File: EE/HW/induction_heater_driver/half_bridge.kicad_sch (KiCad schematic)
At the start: 7 parts, among them Q1 BSC0702LSATMA1, Q2 IRFB7534PBF, U1 UCC5304DWVR

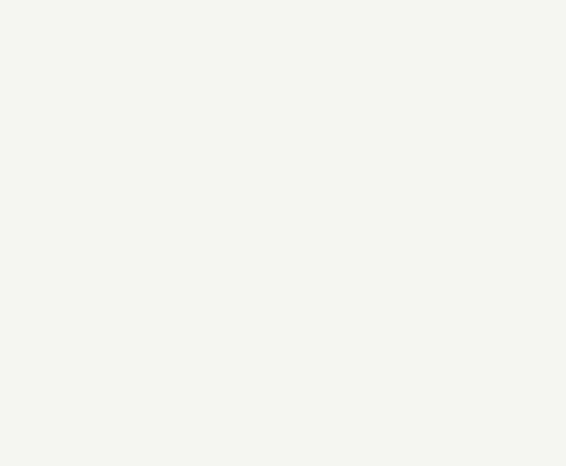
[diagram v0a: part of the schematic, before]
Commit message: imported MAG package from github
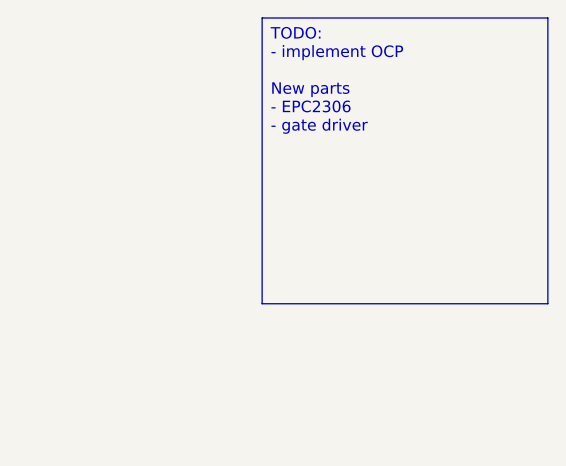
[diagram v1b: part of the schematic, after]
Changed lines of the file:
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@@
 	(generator_version "9.0")
 	(paper "A4")
+	(text_box "TODO:\n- implement OCP\n\nNew parts \n- EPC2306\n- gate driver"
+		(exclude_from_sim no)
+		(at 231.14 30.48 0)
+		(size 31.75 31.75)
+		(margins 0.9525 0.9525 0.9525 0.9525)
+		(stroke
+			(width 0)
+			(type solid)
+		)
+		(fill
+			(type none)
+		)
+		(effects
+			(font
+				(size 1.27 1.27)
+			)
+			(justify left top)
+		)
+	)
 	(symbol
 		(lib_id "peml_passives:CRCW06031R00FKEAHP")
@@
 		)
 		(instances
-			(project ""
+			(project "induction_heater_driver"
 				(path "/4a4d350d-8886-4083-afc6-4b49fb4e1662/876ef4ab-98e7-4587-95f9-89debc1f72ad"
 					(reference "Q2")
@@
 		)
 		(instances
-			(project ""
+			(project "induction_heater_driver"
 				(path "/4a4d350d-8886-4083-afc6-4b49fb4e1662/876ef4ab-98e7-4587-95f9-89debc1f72ad"
 					(reference "R1")
@@
 		)
 		(instances
-			(project ""
+			(project "induction_heater_driver"
 				(path "/4a4d350d-8886-4083-afc6-4b49fb4e1662/876ef4ab-98e7-4587-95f9-89debc1f72ad"
 					(reference "C4")
@@
 		)
 		(instances
-			(project ""
+			(project "induction_heater_driver"
 				(path "/4a4d350d-8886-4083-afc6-4b49fb4e1662/876ef4ab-98e7-4587-95f9-89debc1f72ad"
 					(reference "U1")
@@
 		)
 		(instances
-			(project ""
+			(project "induction_heater_driver"
 				(path "/4a4d350d-8886-4083-afc6-4b49fb4e1662/876ef4ab-98e7-4587-95f9-89debc1f72ad"
 					(reference "C3")
@@
 		)
 		(instances
-			(project ""
+			(project "induction_heater_driver"
 				(path "/4a4d350d-8886-4083-afc6-4b49fb4e1662/876ef4ab-98e7-4587-95f9-89debc1f72ad"
 					(reference "Q1")
